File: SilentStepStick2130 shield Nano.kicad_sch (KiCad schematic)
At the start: 8 parts, among them J1 Conn_01x04_Socket, J2 Conn_01x04_Socket, J5 Conn_01x03, U1 TMC2130_SILENTSTEPSTICK, U2 TMC2130_SILENTSTEPSTICK

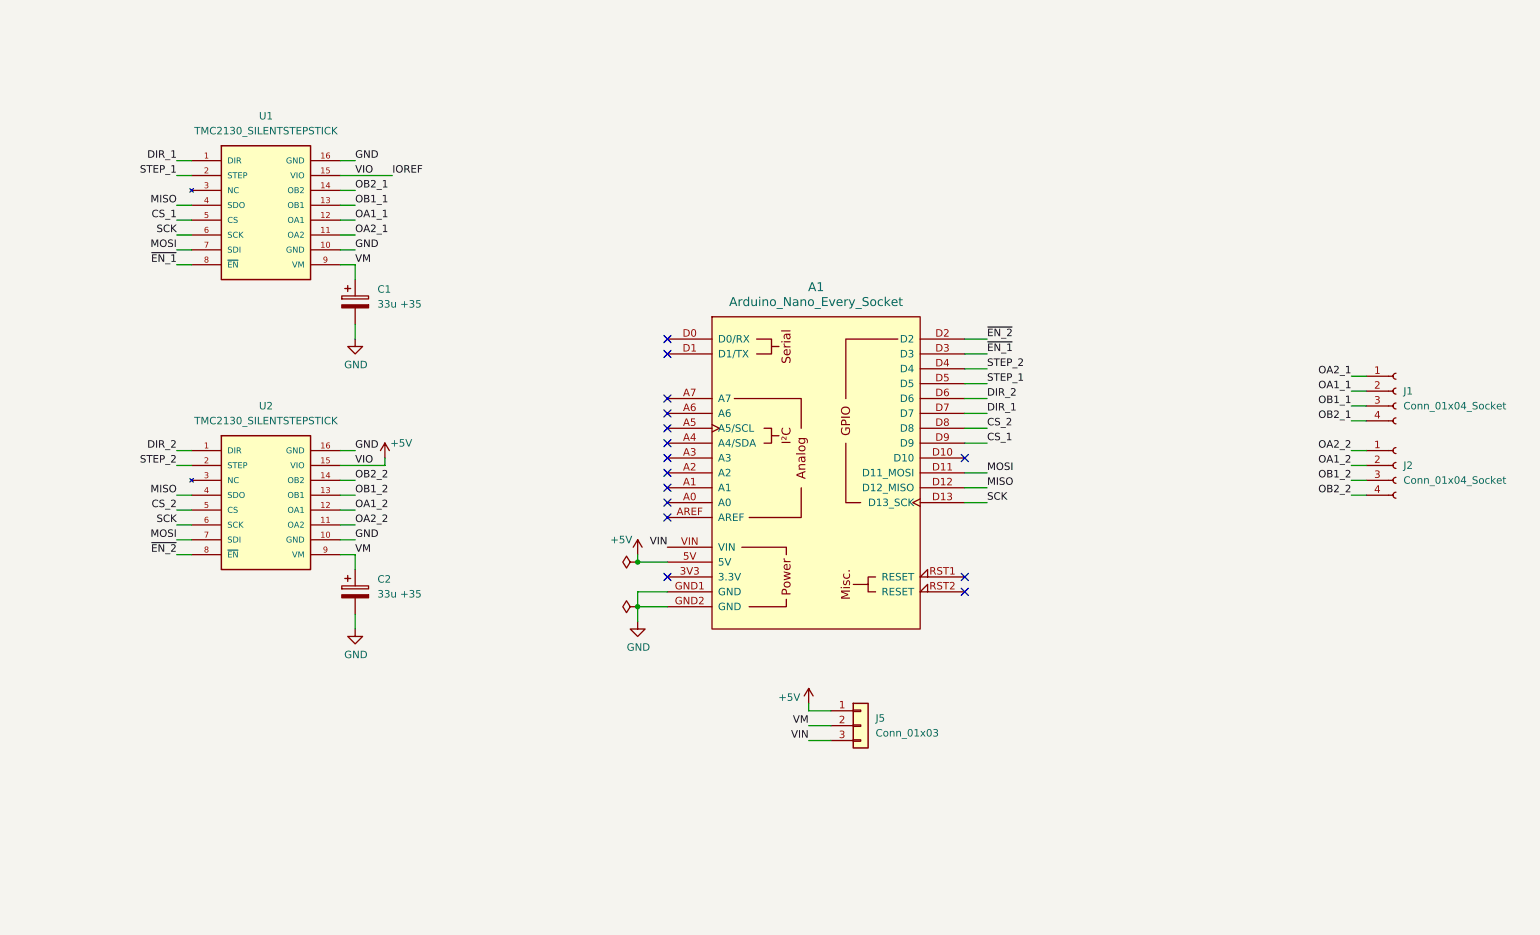
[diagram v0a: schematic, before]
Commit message: redo, nano on the wrong side (can work with headerless nano)
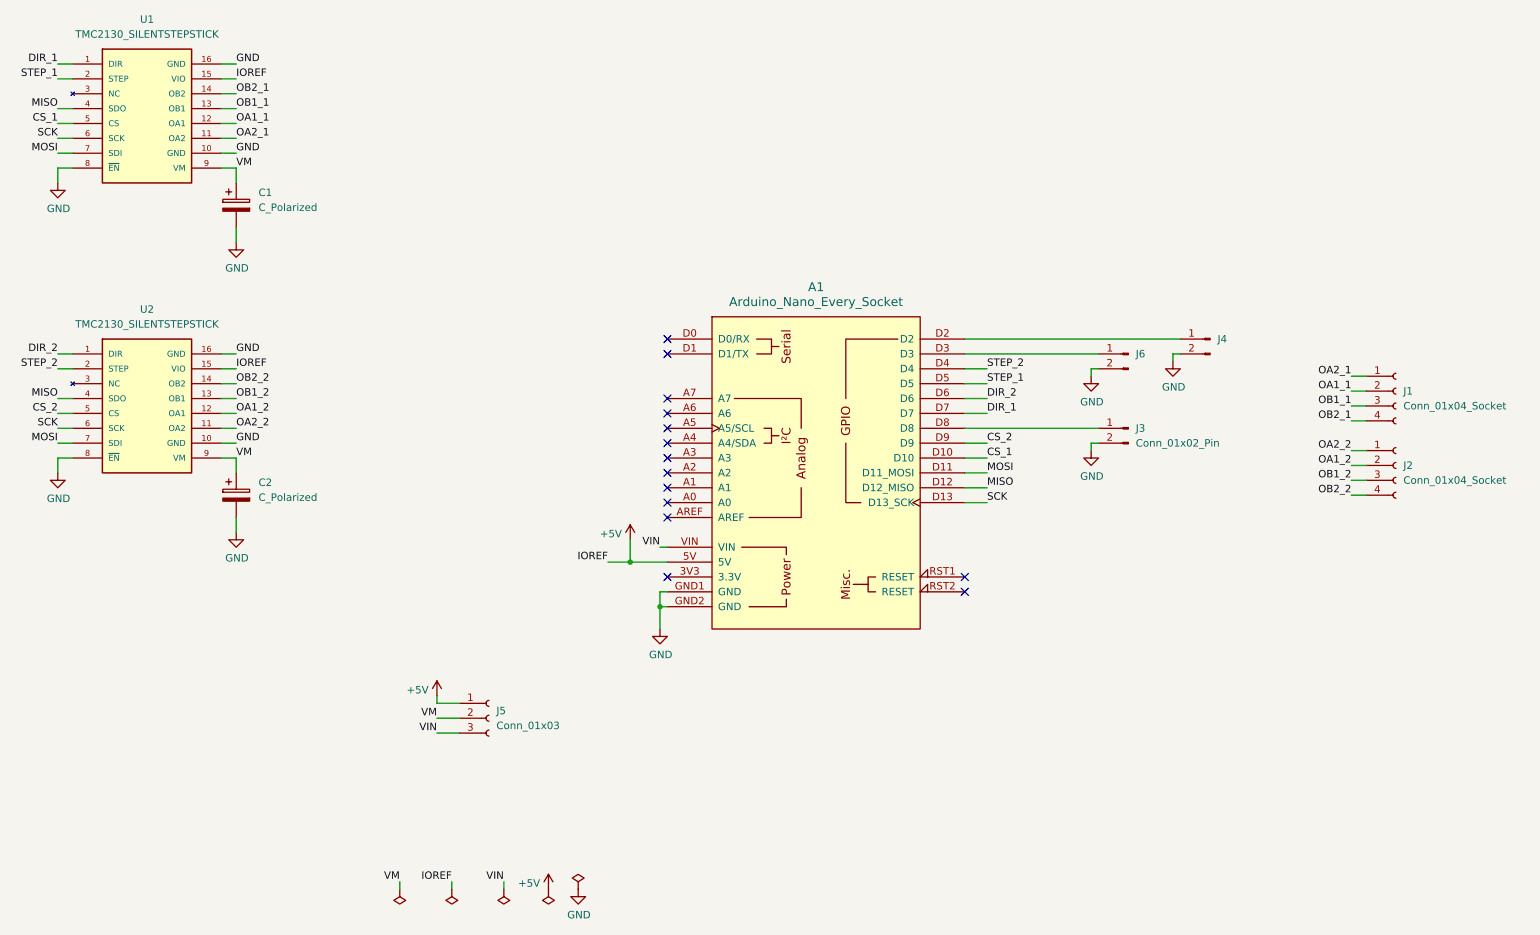
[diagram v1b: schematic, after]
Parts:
- removed J5: Conn_01x03, Connector_PinHeader_2.54mm:PinHeader_1x03_P2.54mm_Vertical, symbol PCM_4ms_Connector:Conn_01x03
- added J3, J4, J6: Conn_01x02_Pin, Connector_JST:JST_XA_S02B-XASK-1_1x02_P2.50mm_Horizontal, symbol Connector:Conn_01x02_Pin
- added J5: Conn_01x03, Connector_PinHeader_2.54mm:PinHeader_1x03_P2.54mm_Vertical, symbol Connector:Conn_01x03_Socket
- A1: footprint LibPersoNadj:Arduino_Nano_Every_Shield -> PCM_arduino-library:Arduino_Nano_Every_Socket
- C1, C2: value 33u +35 -> C_Polarized
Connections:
- net +5V: now also J5.1 (Pin_1)
- net CS_1: now also A1.D10; no longer A1.D9
- net CS_2: now also A1.D9; no longer A1.D8
- net GND: now also U1.8 (~{EN}), U2.8 (~{EN}), J3.2 (Pin_2), J4.2 (Pin_2), J6.2 (Pin_2)
- net VIN: now also J5.3 (Pin_3)
- net VM: now also J5.2 (Pin_2)
- net ~{EN_1}: no longer names the net of A1.D3
- net ~{EN_1}: now also J6.1 (Pin_1); no longer U1.8 (~{EN})
- net ~{EN_2}: no longer names the net of A1.D2
- net ~{EN_2}: now also J4.1 (Pin_1); no longer U2.8 (~{EN})
- new net: A1.D8, J3.1 (Pin_1)
- no-connect marks 15 -> 14
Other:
- moved on the sheet: C1, C2, U1, U2

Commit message: v1
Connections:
- net OA1_1: now also J1.3 (Pin_3); no longer J1.2 (Pin_2)
- net OA1_2: now also J2.3 (Pin_3); no longer J2.2 (Pin_2)
- net OA2_1: now also J1.4 (Pin_4); no longer J1.1 (Pin_1)
- net OA2_2: now also J2.4 (Pin_4); no longer J2.1 (Pin_1)
- net OB1_1: now also J1.2 (Pin_2); no longer J1.3 (Pin_3)
- net OB1_2: now also J2.2 (Pin_2); no longer J2.3 (Pin_3)
- net OB2_1: now also J1.1 (Pin_1); no longer J1.4 (Pin_4)
- net OB2_2: now also J2.1 (Pin_1); no longer J2.4 (Pin_4)
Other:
- note added: "For 23HD56001Y-21B Yellow Blue Green Red"
- moved on the sheet: J1, J2
